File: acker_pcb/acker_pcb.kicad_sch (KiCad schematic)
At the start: 7 parts, among them J1 XT60, J2 servo_header, J3 DC barrel jack, U1 Buck_Module, U2 Buck_Module, U3 dc_motor_controller

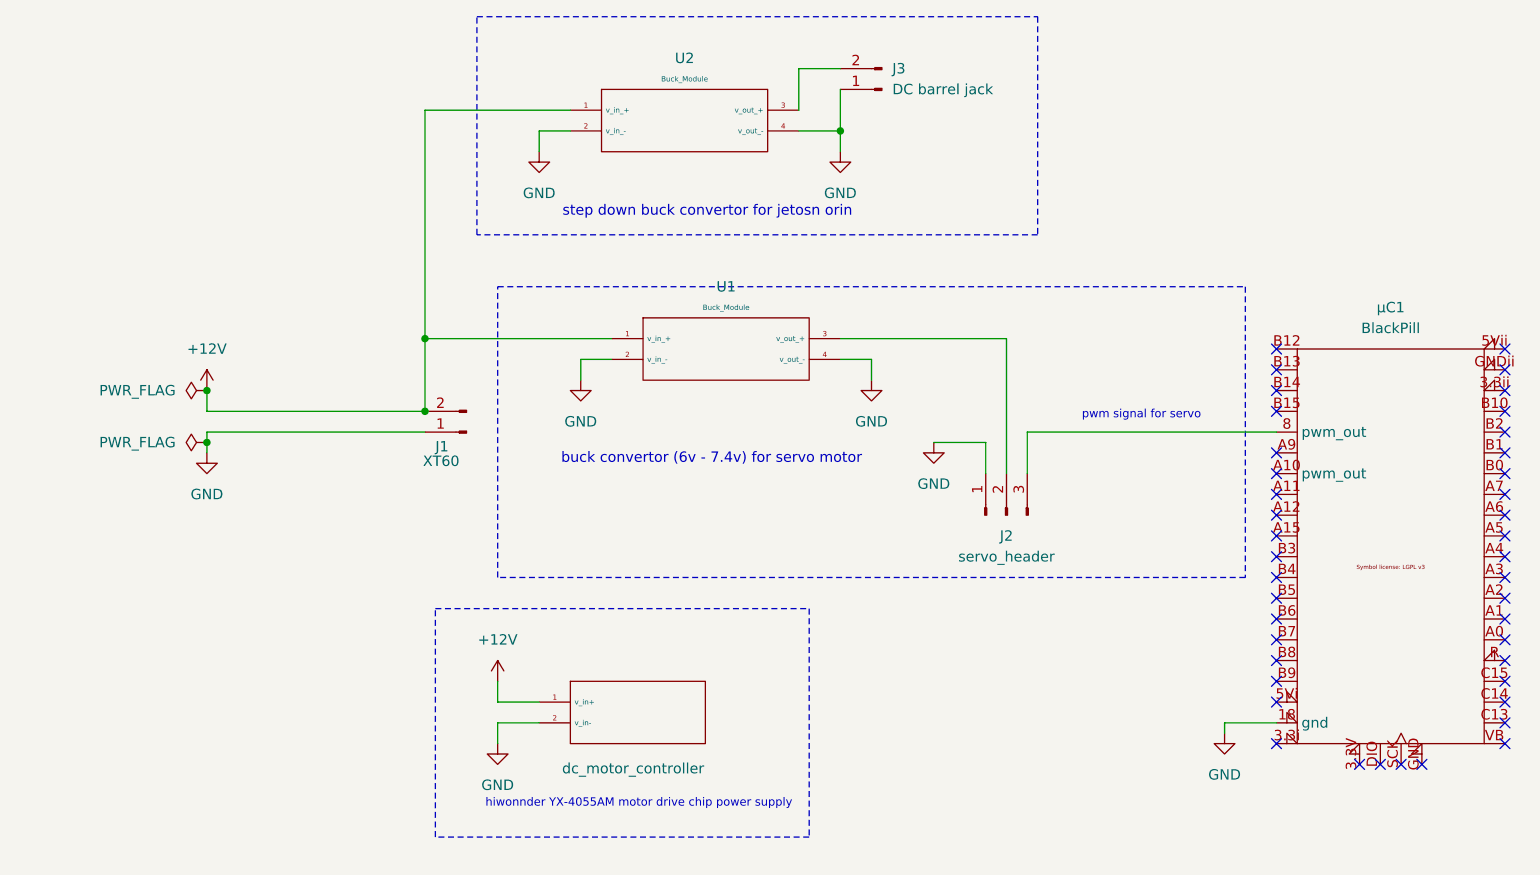
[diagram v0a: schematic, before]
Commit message: added switch and buck footprints
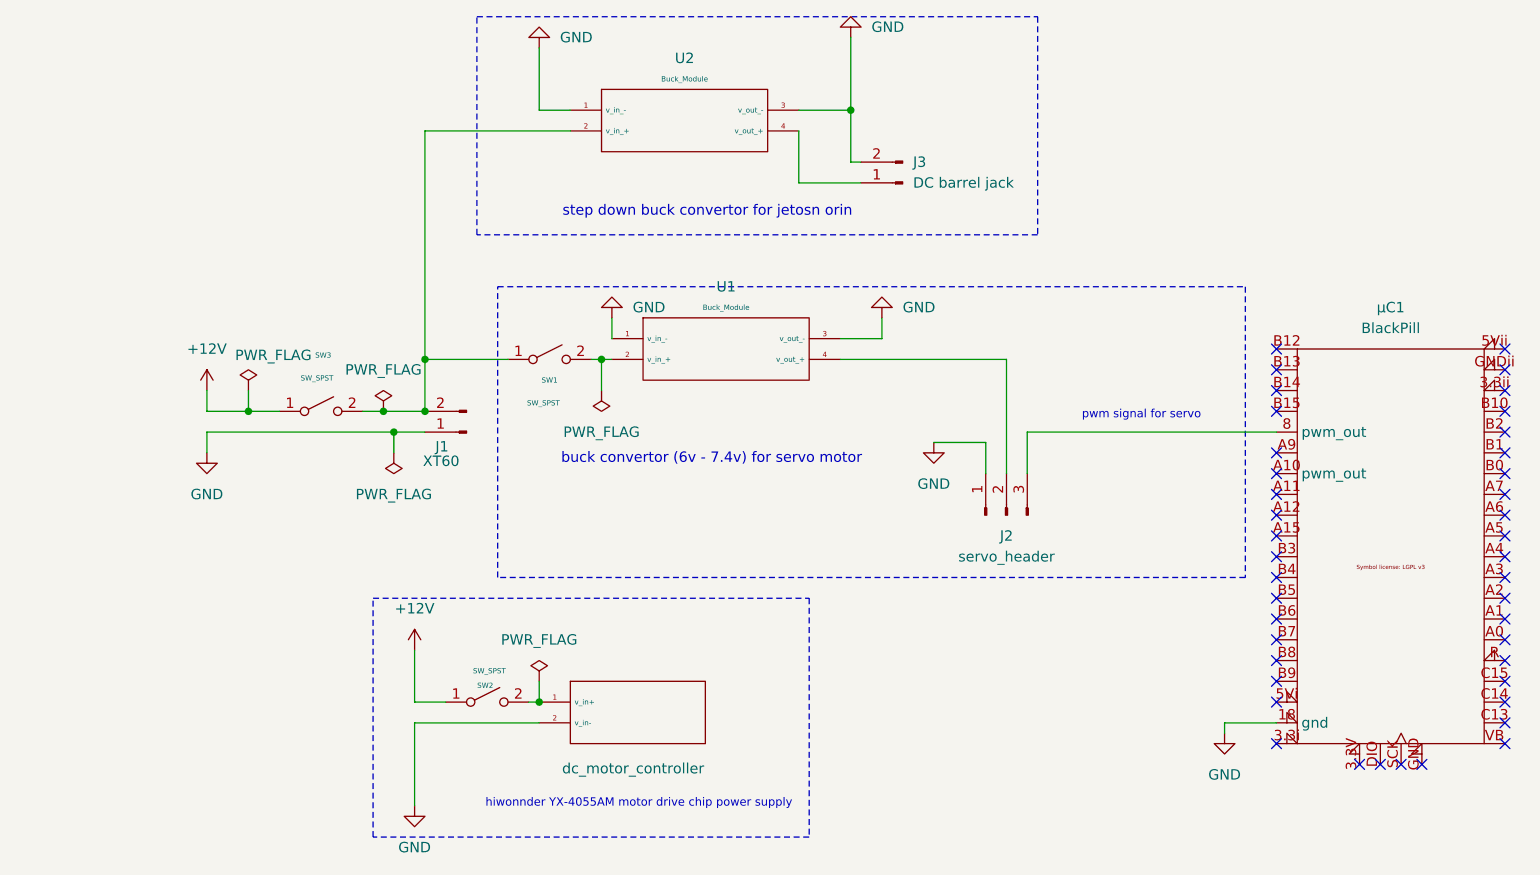
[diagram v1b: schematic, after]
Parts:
- added SW1, SW2, SW3: SW_SPST, acker_chassis:spst_switch, symbol Switch:SW_SPST
- U1: footprint acker_chassis:YX-4055AM motor drive chip -> acker_chassis:XL4015 Buck
- U2: footprint acker_chassis:YX-4055AM motor drive chip -> acker_chassis:XL4016 BUCK
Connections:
- net +12V: now also SW2.1 (A), SW3.1 (A); no longer J1.2 (bat_-), U1.1 (v_in_+), U2.1 (v_in_+), U3.1 (v_in+)
- net GND: now also J3.2 (Pin_2), U1.1 (v_in_-), U1.3 (v_out_-), U2.1 (v_in_-), U2.3 (v_out_-); no longer J3.1 (Pin_1), U1.2 (v_in_-), U1.4 (v_out_-), U2.2 (v_in_-), U2.4 (v_out_-)
- net at J2.2 (servo_power): now also U1.4 (v_out_+); no longer U1.3 (v_out_+)
- new net: SW2.2 (B), U3.1 (v_in+)
- new net: J1.2 (bat_-), SW1.1 (A), SW3.2 (B), U2.2 (v_in_+)
- new net: SW1.2 (B), U1.2 (v_in_+)
- new net: J3.1 (Pin_1), U2.4 (v_out_+)
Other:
- moved on the sheet: J3

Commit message: corrected the switch
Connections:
- net +12V: now also J1.2 (bat_-); no longer SW2.1 (A)
- net GND: now also U1.2 (v_in_-), U1.4 (v_out_-); no longer U1.1 (v_in_-), U1.3 (v_out_-)
- net at J2.2 (servo_power): now also U1.3 (v_out_+); no longer U1.4 (v_out_+)
- net at SW1.1 (A), SW3.2 (B), U2.2 (v_in_+): now also SW2.1 (A); no longer J1.2 (bat_-)
- net at SW1.2 (B): now also U1.1 (v_in_+); no longer U1.2 (v_in_+)
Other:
- moved on the sheet: J1, SW1, SW3
